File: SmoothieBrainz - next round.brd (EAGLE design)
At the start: 101 x 101 mm, 232 parts, among them IC1 LPC1769, IC7 74LVC1G04, Q1 BSL207SP, Q2 12MHz, SW1 SW_TACT_4P_B, SW3 SW_TACT_4P_B, T1 BC817, U3 USD-SOCKETUSD, X1 MSTBA2, X14 USBPTH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

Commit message: Added VMOT indicator led
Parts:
- added LED12: VMOT, led:SML0603
- added R57: 1.5k, resistor:R0603
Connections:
- new net N$23: LED12.C, R57.1
- net 24V: now also R57.2
- net GND: now also LED12.A
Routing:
- net 24V: track 286.4 -> 316.7 mm, vias 3 -> 4
- net ISP_BOOT: track 50.0 -> 53.5 mm
- net GND: track 799.5 -> 800.8 mm

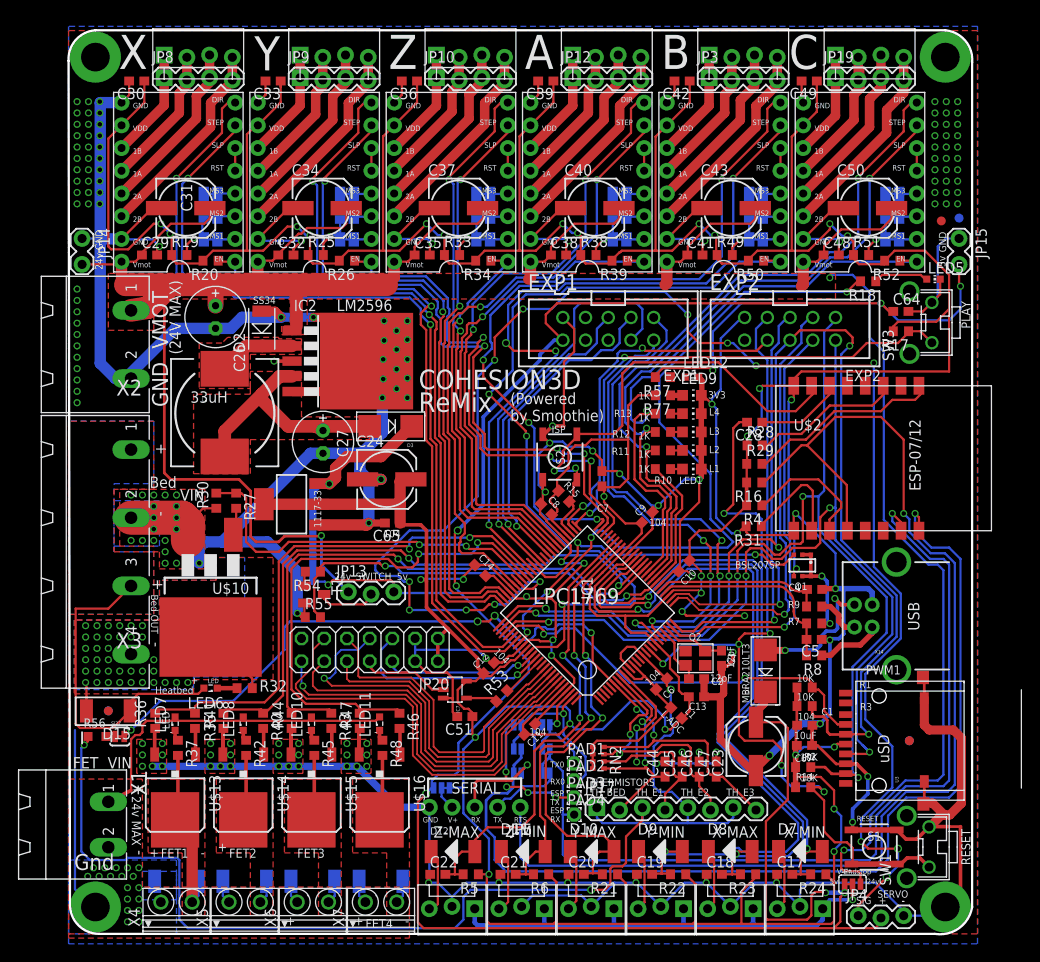
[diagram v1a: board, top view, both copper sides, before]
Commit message: More Cleanup.  Added Headers to Mosfet outputs
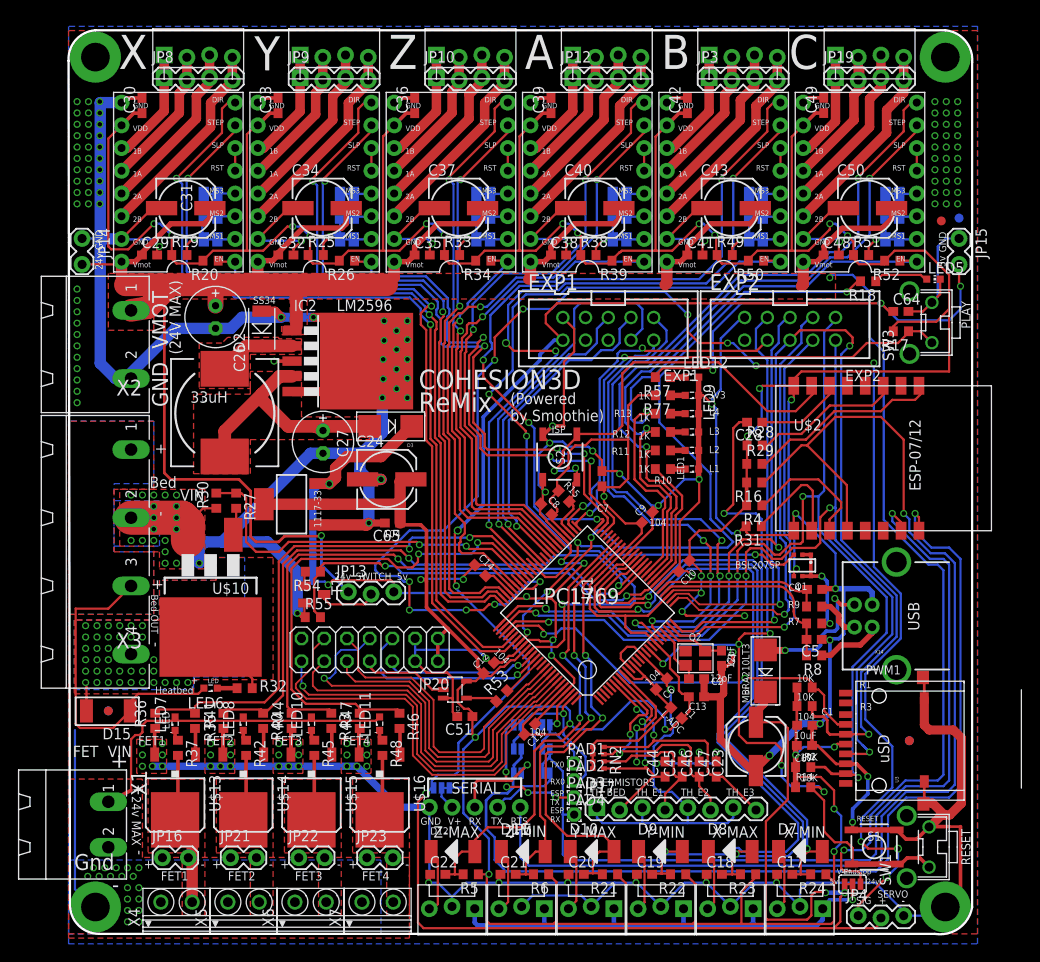
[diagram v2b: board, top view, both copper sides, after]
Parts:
- removed D13, D14, D5, D6: M4, semicon-smd-ipc:SOD87
- removed R56: THERM, varistor:CT/CN0603
- removed SJ27: THERM-JUMPER, SparkFun-Retired:SJ_2S-TRACE
- added JP16, JP21, JP22, JP23: (no value), SparkFun-Connectors:1X02_LOCK
- LED1, LED2, LED3, LED4, LED9: device led:CHIP-LED0805 -> led:SML0603
- moved C49 3.17 mm to (84.4, 92.6), turned to 90 degrees
- moved C42 2.81 mm to (69.2, 92.6), turned to 90 degrees
- moved C30 2.81 mm to (8.21, 92.6), turned to 90 degrees
- moved C36 2.81 mm to (38.7, 92.6), turned to 90 degrees
- moved C39 2.81 mm to (53.9, 92.6), turned to 90 degrees
- moved C33 2.80 mm to (23.4, 92.6), turned to 90 degrees
- moved X7 0.38 mm to (34.5, 3.65)
- moved X6 0.25 mm to (27.1, 3.65)
- moved X5 0.13 mm to (19.6, 3.65)
- turned LED1 to 180 degrees
- turned LED2 to 180 degrees
- turned LED3 to 180 degrees
- turned LED4 to 180 degrees
- turned LED9 to 180 degrees
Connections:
- net AGND: no longer R56.1
- net E1-CONTROL: now also JP16.2; no longer D5.2
- net E2-CONTROL: now also JP21.2; no longer D6.2
- net E3-CONTROL: now also JP22.2; no longer D13.2
- net E4-CONTROL: now also JP23.2; no longer D14.2
- net HEATERVIN: now also JP16.1, JP21.1, JP22.1, JP23.1; no longer D13.1, D14.1, D5.1, D6.1
- net TH4: no longer R56.2, SJ27.1, SJ27.2
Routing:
- net AGND: track 157.9 -> 63.8 mm, vias 7 -> 5
- net TH4: track 103.3 -> 30.8 mm, vias 6 -> 2
- net 3.3V: track 691.8 -> 671.8 mm
- net HEATERVIN: track 47.4 -> 39.6 mm
- net E4-CONTROL: track 9.95 -> 7.34 mm
- net E3-CONTROL: track 9.95 -> 7.34 mm
- net E1-CONTROL: track 19.9 -> 17.3 mm
- net E2-CONTROL: track 9.95 -> 7.34 mm
- net N$23: track 0.00 -> 1.65 mm
- net GND: track 800.8 -> 799.3 mm
- net STP1: track 88.2 -> 87.4 mm
- net ENET_RXD1: track 37.6 -> 37.1 mm

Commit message: rev2 initial ready
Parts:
- added D13, D14, D16, D4, D5, D6: 1N4148, SparkFun-DiscreteSemi:SOD-323
- D10, D11, D12, D15, D7, D8, D9: value M4 -> 1N4148; device semicon-smd-ipc:SOD87 -> SparkFun-DiscreteSemi:SOD-323
- L1: value (none) -> 39nH
- moved C21 2.57 mm to (48.5, 9.14), turned to 90 degrees
- moved C19 2.54 mm to (63.8, 9.14), turned to 90 degrees
- moved C20 2.52 mm to (56.2, 9.12), turned to 90 degrees
- moved C18 2.51 mm to (71.4, 9.06), turned to 90 degrees
- moved R6 2.48 mm to (53.0, 9.13), turned to 90 degrees
- moved R23 2.48 mm to (75.9, 9.13), turned to 90 degrees
- moved C17 2.47 mm to (79.1, 8.93), turned to 90 degrees
- moved R21 2.43 mm to (60.7, 9.08), turned to 90 degrees
- moved R22 2.42 mm to (68.3, 9.08), turned to 90 degrees
- moved R5 2.40 mm to (45.4, 9.02), turned to 90 degrees
- moved C22 2.39 mm to (40.8, 9.01), turned to 90 degrees
- moved D15 2.29 mm to (6.35, 26.2)
- moved R24 2.27 mm to (83.5, 8.91), turned to 90 degrees
- moved U$17 1.27 mm to (4.45, 23.7)
- moved U$20 1.27 mm to (4.45, 23.7)
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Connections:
- net 24V: now also D14.C
- net 5V: now also D16.C
- net E1-CONTROL: now also D4.A
- net E2-CONTROL: now also D5.A
- net E3-CONTROL: now also D6.A
- net E4-CONTROL: now also D13.A
- net HEATBED-CONTROL: now also D15.A; no longer D15.2
- net HEATBEDVIN: now also D15.C; no longer D15.1
- net HEATERVIN: now also D13.C, D4.C, D5.C, D6.C
- net N$11: now also D8.C; no longer D8.1
- net N$13: now also D7.C; no longer D7.1
- net N$16: now also D12.C; no longer D12.1
- net N$4: now also D11.C; no longer D11.1
- net N$5: now also D10.C; no longer D10.1
- net N$56: now also D14.A, D16.A
- net N$7: now also D9.C; no longer D9.1
- net X_MAX: now also D8.A; no longer D8.2
- net X_MIN: now also D7.A; no longer D7.2
- net Y_MAX: now also D10.A; no longer D10.2
- net Y_MIN: now also D9.A; no longer D9.2
- net Z_MAX: now also D12.A; no longer D12.2
- net Z_MIN: now also D11.A; no longer D11.2
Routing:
- net GND: track 799.3 -> 815.1 mm, vias 179 -> 187
- net HEATERVIN: track 39.6 -> 52.7 mm
- net 3.3V: track 671.8 -> 681.5 mm
- net Y_MAX: track 53.2 -> 45.6 mm
- net N$56: track 6.66 -> 10.8 mm
- net HEATBEDVIN: track 37.1 -> 33.3 mm
- net RTS: track 134.4 -> 136.8 mm
- net 5V: track 283.6 -> 285.9 mm
- net Z_MIN: track 47.2 -> 44.9 mm
- net Y_MIN: track 88.4 -> 86.2 mm
- net 24V: track 316.5 -> 318.6 mm
- net Z_MAX: track 52.4 -> 50.3 mm
- net N$13: track 7.19 -> 5.73 mm
- net X_MAX: track 79.9 -> 78.7 mm
- net N$16: track 7.34 -> 6.21 mm
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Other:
- board text added: "ETHERNET"
- board text added: "EXP"
- board text added: "Sig"
- board text added: "rev2"
